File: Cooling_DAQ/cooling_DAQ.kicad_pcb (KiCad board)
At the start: 2 copper layers, 30 x 50 mm, 50 parts, among them J1 Conn_02x10_Odd_Even, J7 USB_C_Receptacle_USB2.0_16P, Q1 2N7002, Q2 2N7002, SW1 SW_SPST, U1 STM32F103C8Tx, U2 AP2204K-ADJ, U3 AP2204K-ADJ, U4 SN65HVD256D, Y1 8M, Y2 32.768k

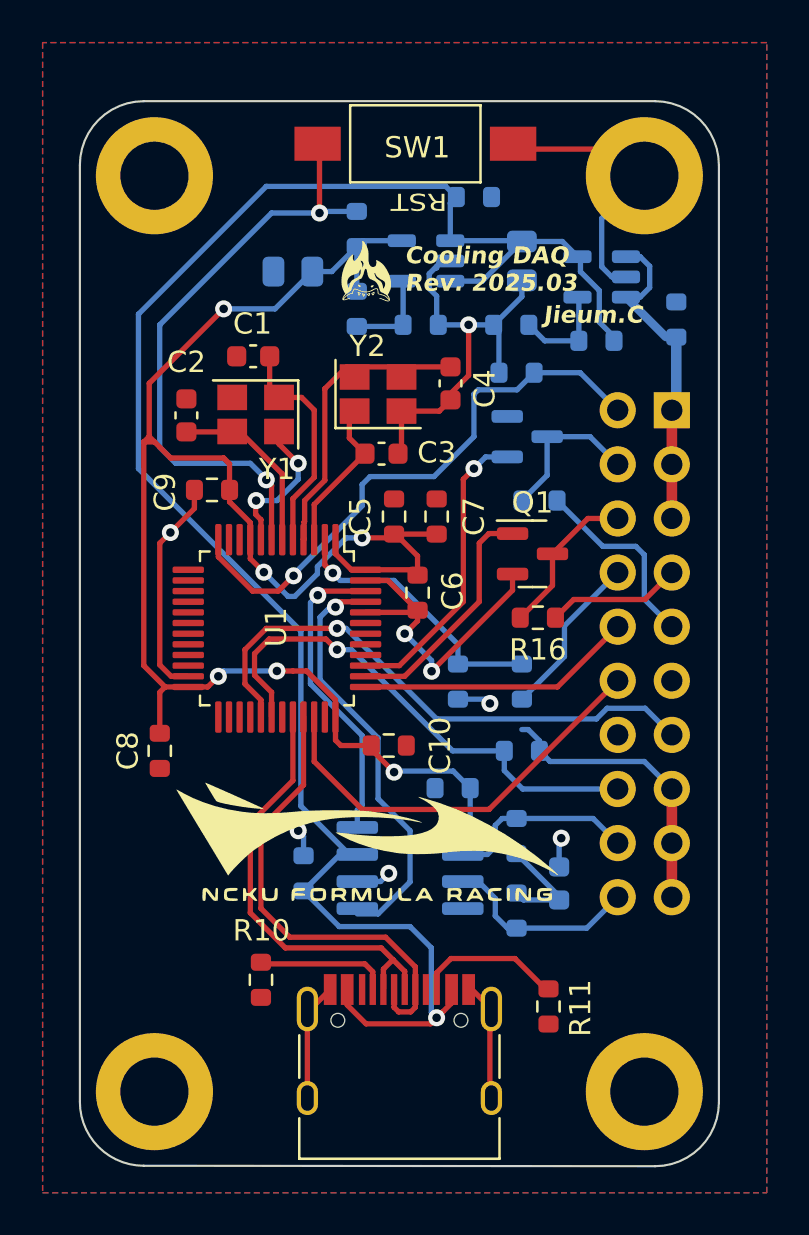
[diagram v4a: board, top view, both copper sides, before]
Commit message: fix: improve pcb layout
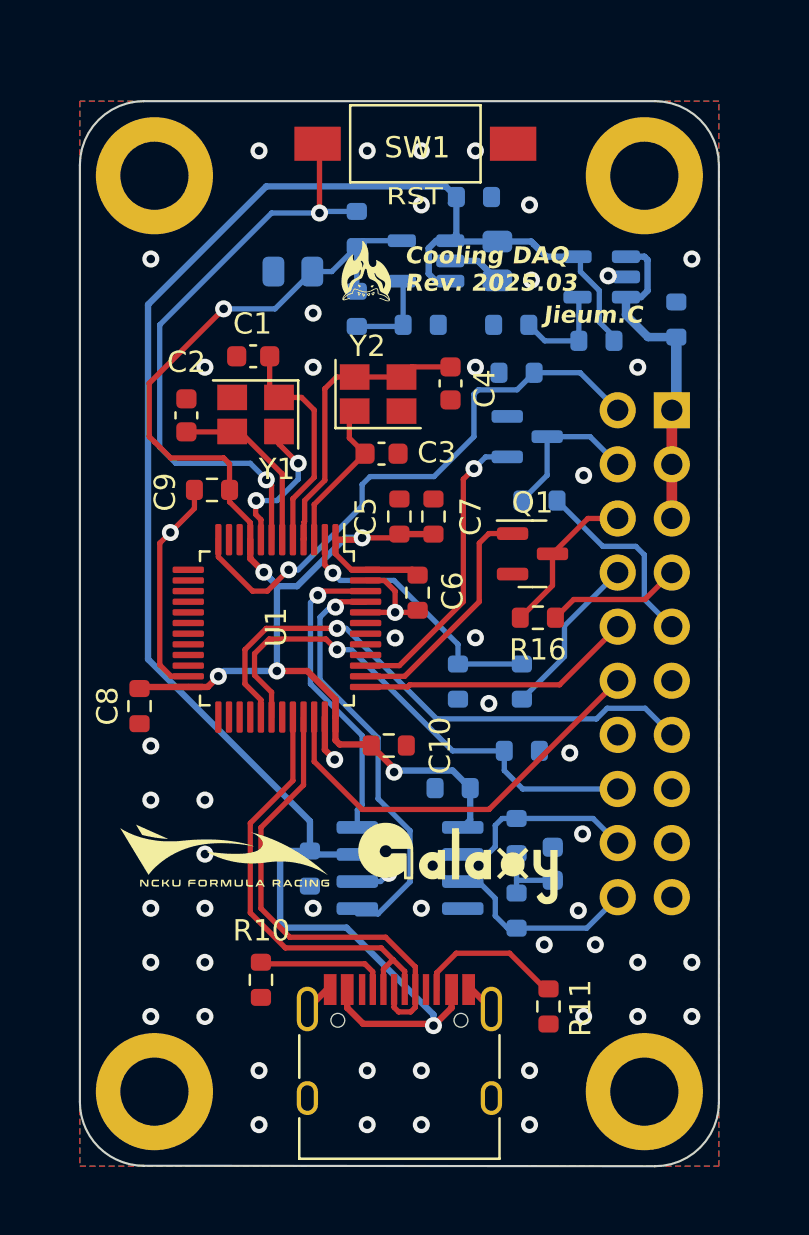
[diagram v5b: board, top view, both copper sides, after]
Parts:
- removed the G*** at (145.5, 128.8)
- added G***: LOGO, logo:nckufs_logo_10mm, F.Cu at (138.8, 129.4)
- added G***: LOGO, logo:galaxy_logo_10mm, F.Cu at (149.8, 129.8)
- moved C8 2.30 mm to (134.8, 122.4)
- moved C13 1.15 mm to (151.6, 101.5)
- moved C15 0.97 mm to (154.2, 129.8)
- moved C16 0.38 mm to (142.8, 130.0), turned to -90 degrees
- moved C5 0.25 mm to (147.0, 113.5)
- moved C7 0.15 mm to (148.6, 113.5)
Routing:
- net GND: track 96.0 -> 32.8 mm, vias 10 -> 56
- net +3V3: track 82.1 -> 71.5 mm
- net +5V: track 85.5 -> 87.3 mm
- net Net-(C15-Pad1): track 5.39 -> 3.56 mm
- net VDC: track 15.3 -> 15.9 mm
